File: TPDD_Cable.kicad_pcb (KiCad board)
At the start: 2 copper layers, 10.6 x 12.7 mm, 5 parts, among them J1 Wire Solder Pads, J2 TPDD, Q1 DTA114EKA, Q2 DTA114EKA, Q3 DTA114EKA

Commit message: pcbway limits, readme
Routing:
- net /SG: track 16.8 -> 16.1 mm
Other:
- net class Default: clearance 0.16 -> 0.2; trace_width 0.16 -> 0.2; via_dia 0.42 -> 0.5; via_drill 0.26 -> 0.3
- rule trace_clearance: 0.16 -> 0.2
- rule trace_min: 0.16 -> 0.2
- rule via_min_drill: 0.26 -> 0.3
- rule via_min_size: 0.42 -> 0.5

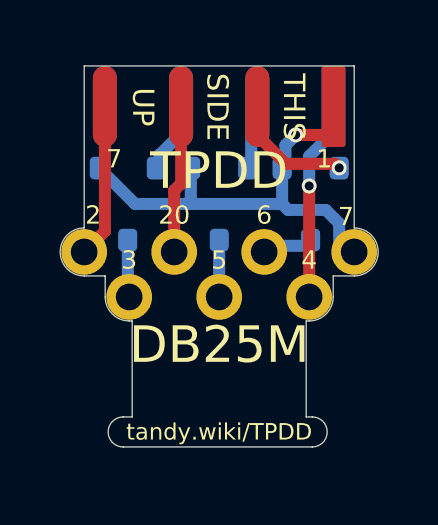
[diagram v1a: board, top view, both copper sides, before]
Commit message: bigger 2x4 solder pads, smaller wire holes
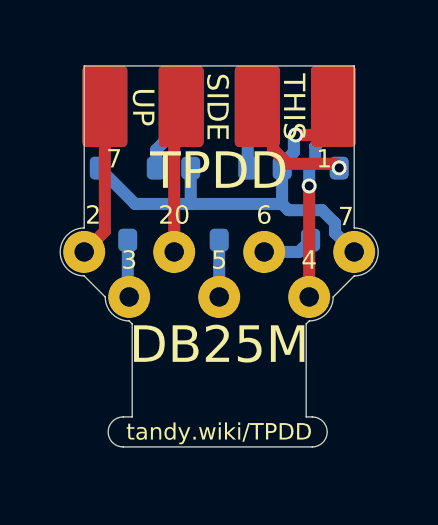
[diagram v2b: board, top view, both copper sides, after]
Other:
- outline, holes or cut-outs redrawn

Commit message: adjust board outline
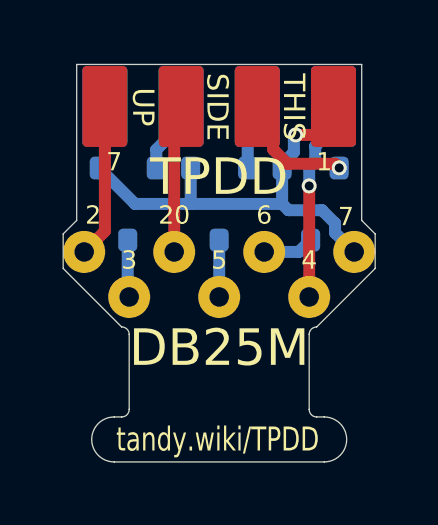
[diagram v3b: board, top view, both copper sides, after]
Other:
- board size 10.6 x 12.7 mm -> 10.4 x 13.2 mm
- board text added: "Q* DTA114EKA"
- board text removed: "Q*: DTA114EKA"
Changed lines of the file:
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@@
-(kicad_pcb (version 20171130) (host pcbnew 5.1.9-73d0e3b20d~88~ubuntu20.10.1)
+(kicad_pcb (version 20171130) (host pcbnew 5.1.10-88a1d61d58~88~ubuntu20.10.1)
   (general
     (thickness 1.6)
-    (drawings 42)
+    (drawings 44)
     (tracks 48)
     (zones 0)
@@
   (title_block
     (title "TPDD Cable")
-    (date 2021-04-26)
-    (rev 003)
+    (date 2021-04-27)
+    (rev 004)
     (company b.kenyon.w@gmail.com)
   )
@@
       (drillshape 0)
       (scaleselection 1)
-      (outputdirectory "GERBER_TPDD_Cable"))
+      (outputdirectory "GERBER_TPDD_Cable_004"))
   )
   (net 0 "")
@@
       (effects (font (size 0.4572 0.4572) (thickness 0.00254)))
     )
-    (fp_text user 8 (at -7.0866 1.7564 unlocked) (layer B.SilkS)
+    (fp_text user 8 (at -7.0866 1.85 unlocked) (layer B.SilkS)
       (effects (font (size 0.6096 0.6096) (thickness 0.0762)) (justify mirror))
     )
-    (fp_text user 2 (at -0.5334 1.7564 unlocked) (layer B.SilkS)
+    (fp_text user 2 (at -0.5334 1.85 unlocked) (layer B.SilkS)
       (effects (font (size 0.6096 0.6096) (thickness 0.0762)) (justify mirror))
     )
-    (fp_text user 7 (at -7.31 1.75 unlocked) (layer F.SilkS)
+    (fp_text user 7 (at -7.31 1.85 unlocked) (layer F.SilkS)
       (effects (font (size 0.6096 0.6096) (thickness 0.0762)))
     )
-    (fp_text user 1 (at -0.31 1.75 unlocked) (layer F.SilkS)
+    (fp_text user 1 (at -0.31 1.85 unlocked) (layer F.SilkS)
       (effects (font (size 0.6096 0.6096) (thickness 0.0762)))
     )
@@
       (effects (font (size 1.2065 1.2065) (thickness 0.1016)) (justify right top mirror))
     )
+    (fp_line (start -0.762 -1.516) (end 0.762 -1.516) (layer B.SilkS) (width 0.0508))
+    (fp_line (start -0.762 1.524) (end 0.762 1.524) (layer B.SilkS) (width 0.0508))
+    (fp_line (start -0.762 1.524) (end -0.762 -1.516) (layer B.SilkS) (width 0.0508))
     (fp_line (start 0.762 1.524) (end 0.762 -1.516) (layer B.SilkS) (width 0.0508))
-    (fp_line (start -0.762 1.524) (end -0.762 -1.516) (layer B.SilkS) (width 0.0508))
-    (fp_line (start -0.762 1.524) (end 0.762 1.524) (layer B.SilkS) (width 0.0508))
-    (fp_line (start -0.762 -1.516) (end 0.762 -1.516) (layer B.SilkS) (width 0.0508))
     (fp_text user %R (at 0 0) (layer B.Fab) hide
       (effects (font (size 0.5 0.5) (thickness 0.075)) (justify mirror))
@@
       (effects (font (size 1.2065 1.2065) (thickness 0.1016)) (justify right top mirror))
     )
+    (fp_line (start -0.762 -1.516) (end 0.762 -1.516) (layer B.SilkS) (width 0.0508))
+    (fp_line (start -0.762 1.524) (end 0.762 1.524) (layer B.SilkS) (width 0.0508))
+    (fp_line (start -0.762 1.524) (end -0.762 -1.516) (layer B.SilkS) (width 0.0508))
     (fp_line (start 0.762 1.524) (end 0.762 -1.516) (layer B.SilkS) (width 0.0508))
-    (fp_line (start -0.762 1.524) (end -0.762 -1.516) (layer B.SilkS) (width 0.0508))
-    (fp_line (start -0.762 1.524) (end 0.762 1.524) (layer B.SilkS) (width 0.0508))
-    (fp_line (start -0.762 -1.516) (end 0.762 -1.516) (layer B.SilkS) (width 0.0508))
     (fp_text user %R (at 0 0) (layer B.Fab) hide
       (effects (font (size 0.5 0.5) (thickness 0.075)) (justify mirror))
@@
       (effects (font (size 1.2065 1.2065) (thickness 0.1016)) (justify right top mirror))
     )
+    (fp_line (start -0.762 -1.516) (end 0.762 -1.516) (layer B.SilkS) (width 0.0508))
+    (fp_line (start -0.762 1.524) (end 0.762 1.524) (layer B.SilkS) (width 0.0508))
+    (fp_line (start -0.762 1.524) (end -0.762 -1.516) (layer B.SilkS) (width 0.0508))
     (fp_line (start 0.762 1.524) (end 0.762 -1.516) (layer B.SilkS) (width 0.0508))
-    (fp_line (start -0.762 1.524) (end -0.762 -1.516) (layer B.SilkS) (width 0.0508))
-    (fp_line (start -0.762 1.524) (end 0.762 1.524) (layer B.SilkS) (width 0.0508))
-    (fp_line (start -0.762 -1.516) (end 0.762 -1.516) (layer B.SilkS) (width 0.0508))
     (fp_text user %R (at 0 0) (layer B.Fab) hide
       (effects (font (size 0.5 0.5) (thickness 0.075)) (justify mirror))
@@
     )
   )
-  (gr_line (start 141.993 89.4295) (end 142.093 89.5295) (layer Edge.Cuts) (width 0.0127))
-  (gr_line (start 147.993 89.4295) (end 147.893 89.5295) (layer Edge.Cuts) (width 0.0127))
-  (gr_line (start 148.793 88.6295) (end 149.493 87.9295) (layer Edge.Cuts) (width 0.0127))
-  (gr_line (start 141.193 88.6295) (end 140.493 87.9295) (layer Edge.Cuts) (width 0.0127))
-  (gr_arc (start 148.093 93.1295) (end 148.093 93.6295) (angle -180) (layer Edge.Cuts) (width 0.0127))
-  (gr_arc (start 141.793 93.1295) (end 141.793 92.6295) (angle -180) (layer Edge.Cuts) (width 0.0127))
-  (gr_line (start 149.493 86.3295) (end 149.493 80.9295) (layer Edge.Cuts) (width 0.0127))
-  (gr_line (start 140.493 86.3295) (end 140.493 80.9295) (layer Edge.Cuts) (width 0.0127))
-  (gr_arc (start 147.993 88.6295) (end 147.993 89.4295) (angle -90) (layer Edge.Cuts) (width 0.0127))
-  (gr_arc (start 141.993 88.6295) (end 141.193 88.6295) (angle -90) (layer Edge.Cuts) (width 0.0127))
-  (gr_arc (start 140.493 87.1295) (end 140.493 86.3295) (angle -180) (layer Edge.Cuts) (width 0.0127))
-  (gr_arc (start 149.493 87.1295) (end 149.493 87.9295) (angle -180) (layer Edge.Cuts) (width 0.0127))
-  (gr_line (start 147.893 92.6295) (end 147.893 89.5295) (layer Edge.Cuts) (width 0.0127))
-  (gr_line (start 142.093 92.6295) (end 142.093 89.5295) (layer Edge.Cuts) (width 0.0127))
-  (gr_line (start 142.093 92.6295) (end 141.793 92.6295) (layer Edge.Cuts) (width 0.0127))
-  (gr_line (start 147.893 92.6295) (end 148.093 92.6295) (layer Edge.Cuts) (width 0.0127))
-  (gr_line (start 140.493 80.9295) (end 149.493 80.9295) (layer Edge.Cuts) (width 0.0127))
-  (gr_line (start 141.793 93.6295) (end 148.093 93.6295) (layer Edge.Cuts) (width 0.0127))
-  (gr_text tandy.wiki/TPDD (at 144.993 93.1295) (layer F.SilkS)
-    (effects (font (size 0.55 0.55) (thickness 0.05)))
+  (gr_arc (start 148.493 93.3795) (end 148.493 94.1295) (angle -180) (layer Edge.Cuts) (width 0.0127))
+  (gr_arc (start 141.493 93.3795) (end 141.493 92.6295) (angle -180) (layer Edge.Cuts) (width 0.0127))
+  (gr_line (start 139.793 86.5295) (end 140.243 86.0795) (layer Edge.Cuts) (width 0.0127))
+  (gr_line (start 139.793 87.6795) (end 139.793 86.5295) (layer Edge.Cuts) (width 0.0127))
+  (gr_line (start 141.743 89.6295) (end 139.793 87.6795) (layer Edge.Cuts) (width 0.0127))
+  (gr_line (start 150.193 86.5295) (end 149.743 86.0795) (layer Edge.Cuts) (width 0.0127))
+  (gr_line (start 150.193 87.6795) (end 150.193 86.5295) (layer Edge.Cuts) (width 0.0127))
+  (gr_line (start 148.243 89.6295) (end 150.193 87.6795) (layer Edge.Cuts) (width 0.0127))
+  (gr_arc (start 148.243 92.3795) (end 147.993 92.3795) (angle -90) (layer Edge.Cuts) (width 0.0127))
+  (gr_arc (start 141.743 92.3795) (end 141.743 92.6295) (angle -90) (layer Edge.Cuts) (width 0.0127))
+  (gr_arc (start 141.743 89.8795) (end 141.993 89.8795) (angle -90) (layer Edge.Cuts) (width 0.0127))
+  (gr_arc (start 148.243 89.8795) (end 148.243 89.6295) (angle -90) (layer Edge.Cuts) (width 0.0127))
+  (gr_line (start 147.993 89.8795) (end 147.993 92.3795) (layer Edge.Cuts) (width 0.0127))
+  (gr_line (start 149.743 80.8795) (end 149.743 86.0795) (layer Edge.Cuts) (width 0.0127))
+  (gr_line (start 140.243 80.8795) (end 149.743 80.8795) (layer Edge.Cuts) (width 0.0127))
+  (gr_line (start 140.243 86.0795) (end 140.243 80.8795) (layer Edge.Cuts) (width 0.0127))
+  (gr_line (start 141.993 92.3795) (end 141.993 89.8795) (layer Edge.Cuts) (width 0.0127))
+  (gr_line (start 148.493 92.6295) (end 148.243 92.6295) (layer Edge.Cuts) (width 0.0127))
+  (gr_line (start 141.743 92.6295) (end 141.493 92.6295) (layer Edge.Cuts) (width 0.0127))
+  (gr_line (start 141.493 94.1295) (end 148.493 94.1295) (layer Edge.Cuts) (width 0.0127))
+  (gr_text tandy.wiki/TPDD (at 144.943 93.3795) (layer F.SilkS)
+    (effects (font (size 0.8 0.6) (thickness 0.1)))
   )
   (gr_text THIS (at 147.483 82.296 -90) (layer F.SilkS)
@@
     (effects (font (size 0.7112 0.7112) (thickness 0.0762)) (justify mirror))
   )
-  (gr_text "Q*: DTA114EKA" (at 145.018 93.1295) (layer B.SilkS)
-    (effects (font (size 0.6 0.6) (thickness 0.05)) (justify mirror))
-  )
-  (gr_text DB25M (at 144.993 90.2295) (layer F.SilkS)
+  (gr_text "Q* DTA114EKA" (at 145.018 93.3795) (layer B.SilkS)
+    (effects (font (size 0.8 0.7) (thickness 0.1)) (justify mirror))
+  )
+  (gr_text DB25M (at 144.993 90.3295) (layer F.SilkS)
     (effects (font (size 1.2192 1.2192) (thickness 0.1524)))
   )
@@
     (effects (font (size 0.6096 0.6096) (thickness 0.0762)))
   )
-  (gr_text TPDD (at 144.993 84.4295) (layer F.SilkS)
+  (gr_text TPDD (at 144.993 84.6295) (layer F.SilkS)
     (effects (font (size 1.2192 1.2192) (thickness 0.1524)))
   )
